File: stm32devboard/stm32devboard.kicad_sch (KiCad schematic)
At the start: 44 parts, among them J1 Conn_01x20, J2 Conn_01x20, J3 USB_C_Receptacle_USB2.0, J4 Conn_01x03, SW1 SW_SPST, SW2 SW_SPST, U1 STM32F042C6Tx, U2 AP63203WU, U3 TCAN332, U4 IP4234CZ6,125

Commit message: Fixed DR fixes
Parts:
- removed J4: Conn_01x03, Connector_PinHeader_2.54mm:PinHeader_1x03_P2.54mm_Vertical, symbol Connector_Generic:Conn_01x03
- removed JP1, JP2, JP3: Jumper_2_Open, Jumper:SolderJumper-2_P1.3mm_Open_RoundedPad1.0x1.5mm, symbol Jumper:Jumper_2_Open
- added C15, C16: GCM1885C2A200JA16D, Capacitor_SMD:C_0603_1608Metric, symbol 1u_panel-eagle-import:C-EU0603-C-NOSILK
- added J5: Conn_ARM_JTAG_SWD_10, Connector:Tag-Connect_TC2030-IDC-NL_2x03_P1.27mm_Vertical, symbol Connector:Conn_ARM_JTAG_SWD_10
- added X1: ECS-160-10-36Q-ES-TR, Crystal:Crystal_SMD_2520-4Pin_2.5x2.0mm, symbol 1u_panel-eagle-import:CRYSTAL-WITH-GND
- C11: value DNP -> 0.1u
- C12: value DNP -> 1n
- R2: value 1 -> 0
- R7, R8: value 120 -> 60.4
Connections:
- net +3V3: now also J2.4 (Pin_4), J5.1 (VTref)
- net CAN+: now also R8.1; no longer C12.2
- net CAN-: now also R7.1; no longer C11.2
- net GND: now also C11.2, J2.2 (Pin_2), C15.2, C16.2, J5.3 (GND), J5.5 (GND), J5.9 (GNDDetect), X1.2 (SHIELD), X1.4 (SHIELD); no longer C11.1, R7.2, R8.2
- net PB8: now also R6.1; no longer R6.2
- net PB9: now also R5.1; no longer R5.2
- net PF11: now also J2.3 (Pin_3); no longer J2.4 (Pin_4)
- net RESET: now also J5.10 (~{RESET})
- net SWDIO: now also J5.2 (SWDIO/TMS)
- net SWSCK: now also J5.4 (SWCLK/TCK)
- net USB_SHLD: now also C11.1
- net at U3.1 (TXD): now also R5.2; no longer R5.1
- net at U3.4 (RXD): now also R6.2; no longer R6.1
- net LED: no longer names the net of R4.1, U1.38 (PA15)
- net PF0: no longer names the net of U1.5 (PF0)
- net PF0: now also C15.1, X1.1; no longer J2.2 (Pin_2)
- net PF1: no longer names the net of U1.6 (PF1)
- net PF1: now also C16.1, X1.3 (2); no longer J2.3 (Pin_3)
- new net: C12.2, R7.2, R8.2
- no-connect marks 3 -> 5
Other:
- note added: "3v3"
- note added: "3v3 Regulator"
- note added: "Analog"
- note added: "BOOT"
- note added: "CAN tranceiver"
- note added: "CAN_L, CAN_H"
- note added: "CAN_RX, CAN_TX"
- note added: "Crystal"
- note added: "GPIO"
- note added: "Microcontroller"
- note added: "PWR_EN"
- note added: "RESET"
- note added: "Reset"
- note added: "SWD"
- note added: "USB_DM, USB_DP"
- note added: "VBUS"
- note added: "bootsel"
- company: (none) -> PSAS
- title: (none) -> minTS Microcontroller Devboad
- moved on the sheet: C1, C10, C12, C13, C14, C2, C3, C4, C5, C6, C7, C8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

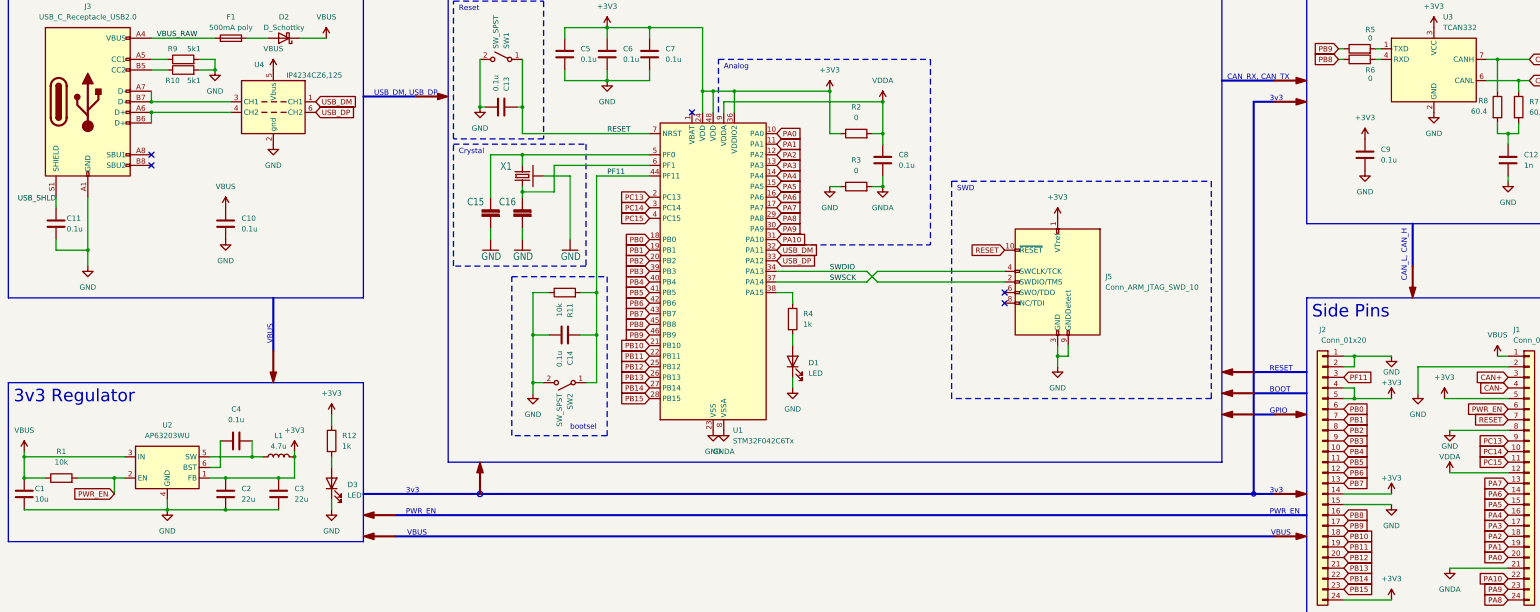
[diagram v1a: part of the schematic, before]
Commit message: Updated BOM and silkscreen
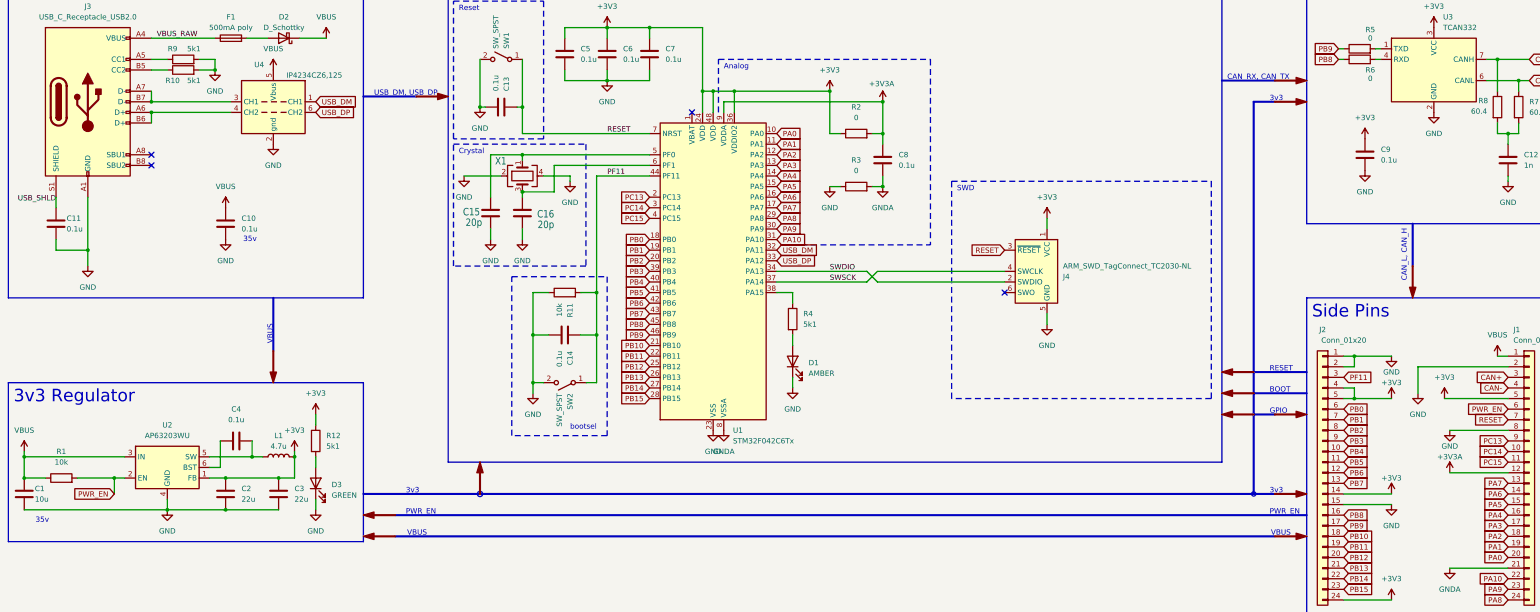
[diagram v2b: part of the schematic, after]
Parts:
- removed J5: Conn_ARM_JTAG_SWD_10, Connector:Tag-Connect_TC2030-IDC-NL_2x03_P1.27mm_Vertical, symbol Connector:Conn_ARM_JTAG_SWD_10
- added J4: ARM_SWD_TagConnect_TC2030-NL, Connector:Tag-Connect_TC2030-IDC-NL_2x03_P1.27mm_Vertical, symbol Connector:Conn_ARM_SWD_TagConnect_TC2030-NL
- C1: DPN (none) -> 490-13248-1-ND; MPN (none) -> GRM188R6YA106MA73D
- C10, C11, C13, C14, C4, C5, C6, C7, C8, C9: DPN (none) -> 1276-1935-1-ND; MPN (none) -> CL10B104KB8NNWC
- C12: DPN (none) -> 732-7927-1-ND; MPN (none) -> CAP CER 1000PF 10V X7R 0603
- C15, C16: value GCM1885C2A200JA16D -> 20p; symbol 1u_panel-eagle-import:C-EU0603-C-NOSILK -> Device:C; DPN (none) -> 490-11157-1-ND; MPN (none) -> GCM1885C2A200JA16D
- C2, C3: DPN (none) -> 1276-1274-1-ND; MPN (none) -> CL10A226MP8NUNE
- D1: value LED -> AMBER; DPN (none) -> 3147-B1911UY--20D000114U1930CT-ND; MPN (none) -> B1911UY--20D000114U1930
- D3: value LED -> GREEN; DPN (none) -> 3147-B1911NG--20D000214U1930CT-ND; MPN (none) -> B1911NG--20D000214U1930
- J1, J2: DPN (none) -> 2057-PH1-20-UA-ND; MPN (none) -> PH1-20-UA
- R1, R11: DPN (none) -> RMCF0603FT10K0CT-ND; MPN (none) -> RMCF0603FT10K0
- R10, R9: DPN (none) -> RMCF0603FT5K10CT-ND; MPN (none) -> RMCF0603FT5K10
- R12, R4: value 1k -> 5k1; DPN (none) -> RMCF0603FT5K10CT-ND; MPN (none) -> RMCF0603FT5K10
- R2, R3, R5, R6: DPN (none) -> RMCF0603ZT0R00CT-ND; MPN (none) -> RMCF0603ZT0R00
- R7, R8: DPN (none) -> RMCF0603FT60R4CT-ND; MPN (none) -> RMCF0603FT60R4
- X1: symbol 1u_panel-eagle-import:CRYSTAL-WITH-GND -> Device:Crystal_GND24; DPN (none) -> XC2181CT-ND; MPN (none) -> ECS-160-10-36Q-ES-TR
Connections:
- net +3V3: now also J4.1 (VCC)
- net GND: now also J4.5 (GND)
- net RESET: now also J4.3 (~{RESET})
- net SWDIO: now also J4.2 (SWDIO)
- net SWSCK: now also J4.4 (SWCLK)
- net VDDA renamed +3V3A
- no-connect marks 5 -> 4
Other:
- note added: "35v"
- moved on the sheet: D3, R12
